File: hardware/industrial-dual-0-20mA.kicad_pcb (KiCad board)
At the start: 2 copper layers, 40 x 40 mm, 40 parts, among them P1 CON-SENSOR2, P2 DEBUG, P3 BOOT, P4 P-PWR-8GN, Q1 FDN5630, U1 XMC1XXX24, U3 MCP3423, U4 DRILL, U5 DRILL, U6 DRILL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

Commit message: fix product name
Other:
- board text added: "Industrial Dual 0-20mA 2.0"
- board text removed: "Industrial 0-20mA 2.0"
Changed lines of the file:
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@@
     (effects (font (size 0.8001 0.8001) (thickness 0.14986)))
   )
-  (gr_text "Industrial 0-20mA\n2.0\n" (at 135.8 58.1 90) (layer F.SilkS)
+  (gr_text "Industrial Dual 0-20mA\n2.0\n" (at 135.8 58.1 90) (layer F.SilkS)
     (effects (font (size 1 1) (thickness 0.15)))
   )

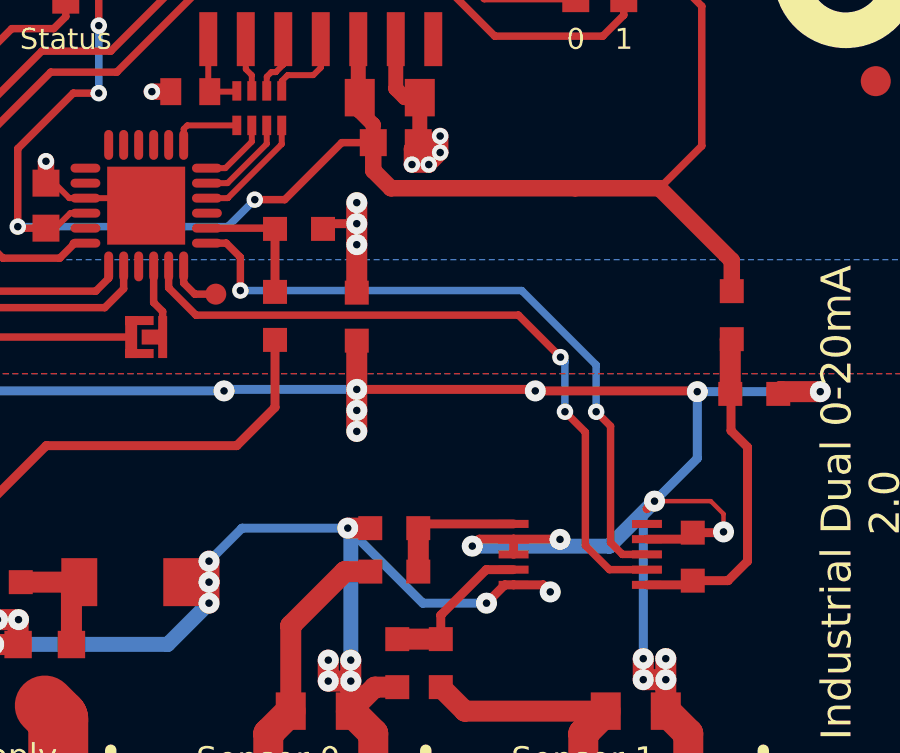
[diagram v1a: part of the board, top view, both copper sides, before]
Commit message: add missing pullup
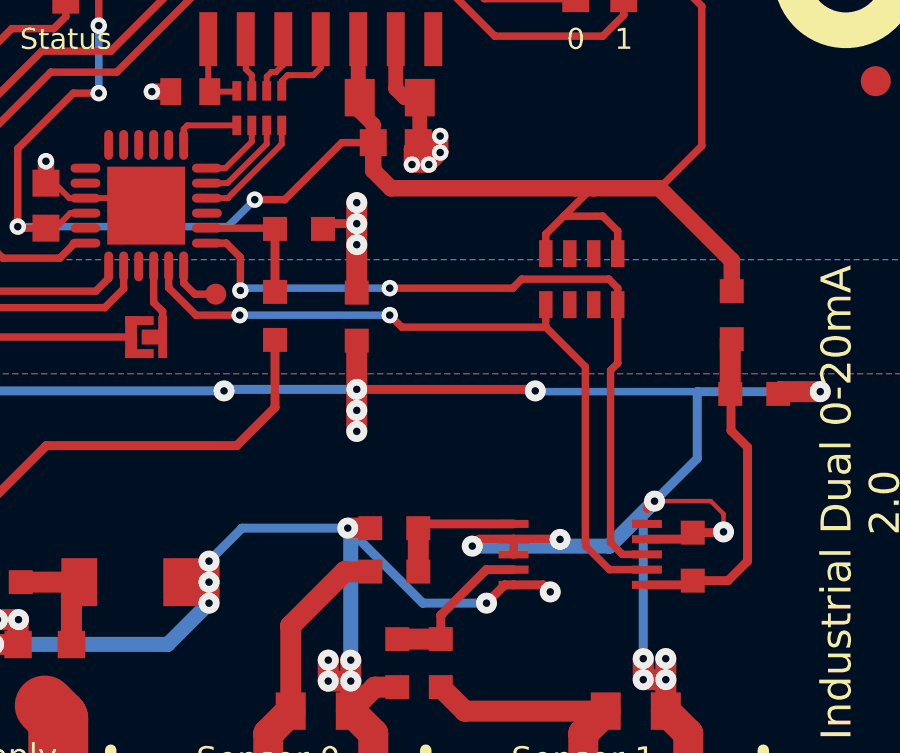
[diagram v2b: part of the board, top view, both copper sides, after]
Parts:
- added RP101: 2k2, kicad-libraries:4X0603, F.Cu at (126.5, 50.6)
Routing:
- net 3V3: track 57.5 -> 63.3 mm
- net SCL: track 22.8 -> 25.2 mm
- net SDA: track 23.7 -> 24.8 mm
- net AGND: vias 29 -> 28
